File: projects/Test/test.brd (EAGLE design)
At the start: 65.8 x 27.6 mm, 45 parts, among them J1 284512-3, Y1 ECS-80-S-4X

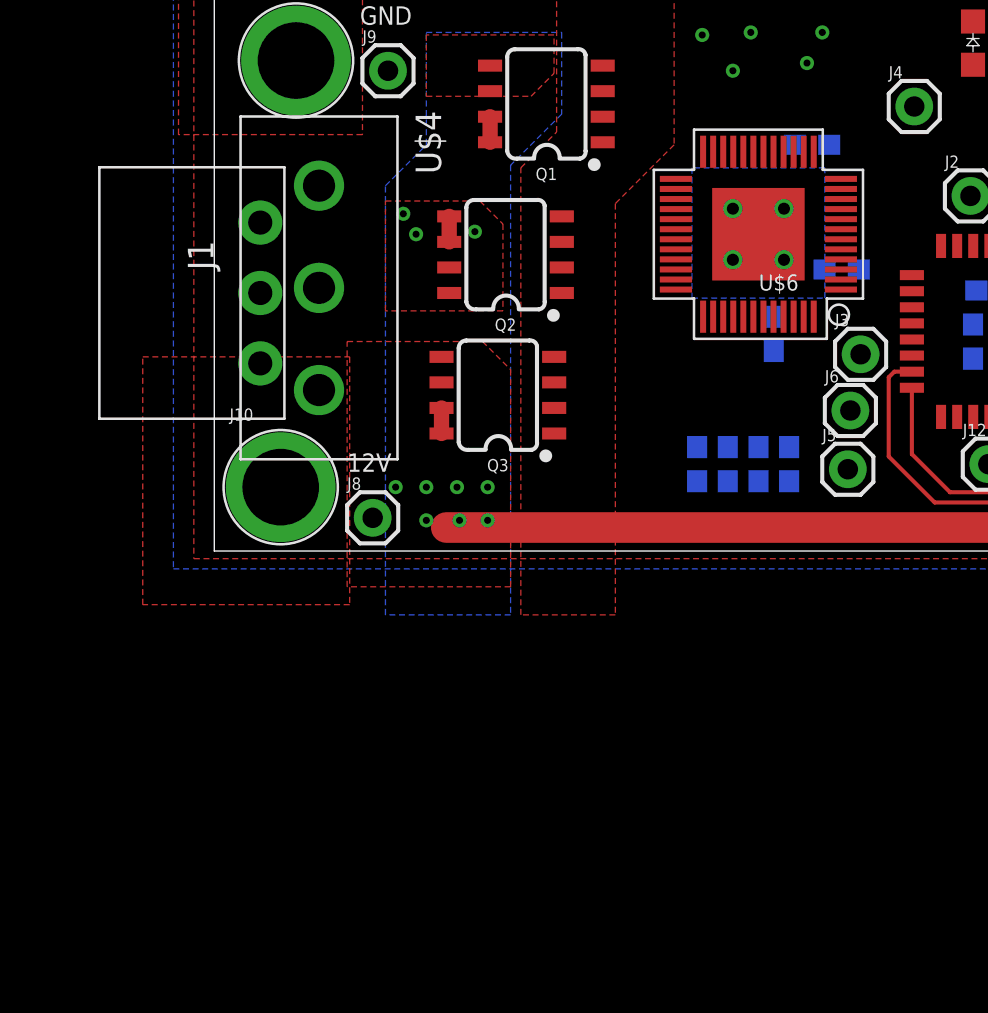
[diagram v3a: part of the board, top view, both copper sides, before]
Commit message: Switch to drv8343
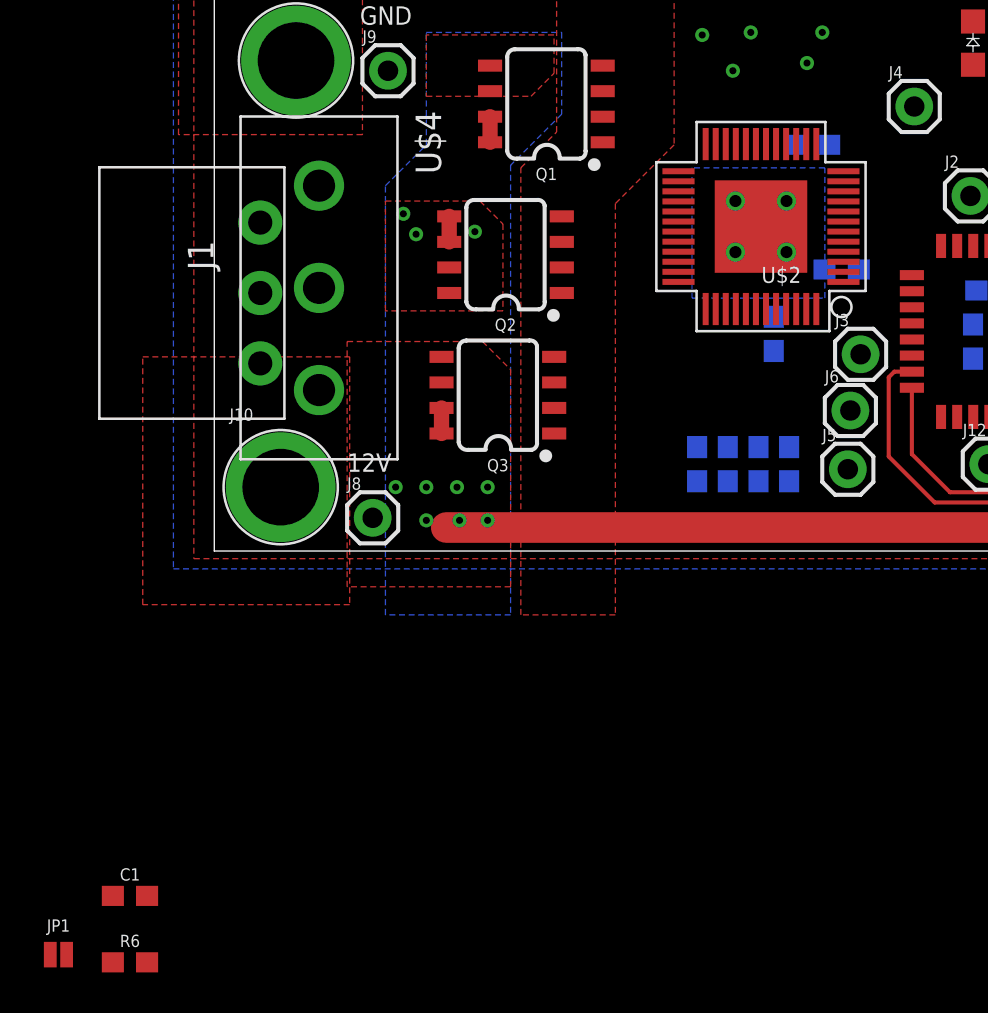
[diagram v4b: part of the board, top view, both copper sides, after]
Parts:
- removed U$6: DRV8340HBOTTOM-PAD, Motor Driver - DRV8340H:48-TQFP-BOTTOM
- added C1: 0.1uF, SparkFun-Capacitors:0603
- added JP1: JUMPER-SMT_2_NO_NO-SILK, SparkFun-Jumpers:SMT-JUMPER_2_NO_NO-SILK
- added R6: 47k, SparkFun-Resistors:0603
- added U$2: DRV8343H, Motor Driver - DRV834xH:48-TQFP-BOTTOM
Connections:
- new net !DIAG: U$2.40
- new net CAL: U$2.37, U$5.27
- new net GAIN: JP1.1, R6.2, U$2.35
- new net SNA: U$2.12
- new net SNB: U$2.13
- new net SNC: U$2.26
- new net SOA: U$2.29, U$5.8
- new net SOB: U$2.28, U$5.9
- new net SOC: U$2.27, U$5.11
- new net SPA: U$2.11
- new net SPB: U$2.14
- new net SPC: U$2.25
- net +3V3: now also C1.1, U$2.30
- net 12V: now also U$2.4, U$2.5; no longer U$6.4, U$6.5
- net 3V3_OUT: now also JP1.2, U$2.39; no longer U$6.39
- net CPH: now also U$2.2; no longer U$6.2
- net CPL: now also U$2.1; no longer U$6.1
- net EN_1: now also U$2.36; no longer U$6.36
- net FAULT_1: now also U$2.31; no longer U$6.31
- net GHA_1: now also U$2.6; no longer U$6.6
- net GHB_1: now also U$2.19; no longer U$6.19
- net GHC_1: now also U$2.20; no longer U$6.20
- net GLA_1: now also U$2.9; no longer U$6.9
- net GLB_1: now also U$2.16; no longer U$6.16
- net GLC_1: now also U$2.23; no longer U$6.23
- net GND: now also C1.2, R6.1, U$2.10, U$2.15, U$2.24, U$2.38, U$2.47, U$2.48, U$2.PAD, U$2.PAD_BOT, U$2.PAD_CON1, U$2.PAD_CON2, U$2.PAD_CON3, U$2.PAD_CON4; no longer U$6.10, U$6.11, U$6.12, U$6.13, U$6.14, U$6.15, U$6.24, U$6.25, U$6.26, U$6.27, U$6.28, U$6.29, U$6.30, U$6.37, U$6.38, U$6.47, U$6.48, U$6.PAD, U$6.PAD_BOT
- net IDRIVE: now also U$2.33; no longer U$6.33
- net INHA_1: now also U$2.41; no longer U$6.41
- net INHB_1: now also U$2.43; no longer U$6.43
- net INHC_1: now also U$2.45; no longer U$6.45
- net INLA_1: now also U$2.42; no longer U$6.42
- net INLB_1: now also U$2.44; no longer U$6.44
- net INLC_1: now also U$2.46; no longer U$6.46
- net MODE: now also U$2.32; no longer U$6.32
- net PHASE_A1: now also U$2.7, U$2.8; no longer U$6.7, U$6.8
- net PHASE_B1: now also U$2.17, U$2.18; no longer U$6.17, U$6.18
- net PHASE_C1: now also U$2.21, U$2.22; no longer U$6.21, U$6.22
- net VDS: now also U$2.34; no longer U$6.34
- net V_CAP_L: now also U$2.3; no longer U$6.3

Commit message: updated board
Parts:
- moved JP1 43.0 mm to (25.3, 7.11), turned to 270 degrees
- moved R6 39.3 mm to (23.0, 7.62)
- moved C1 38.2 mm to (22.9, 9.40), turned to 180 degrees
- moved C17 10.2 mm to (28.7, 23.5), turned to 180 degrees
- moved C15 8.64 mm to (28.8, 25.3)
- moved J3 6.58 mm to (31.0, 2.92)
- moved J7 5.40 mm to (35.7, 20.7)
- moved R7 5.26 mm to (22.9, 8.64), turned to 180 degrees
- moved J4 4.07 mm to (35.8, 17.8)
- moved C16 3.35 mm to (41.8, 11.2)
- moved C14 3.22 mm to (33.4, 15.9), turned to 90 degrees
- moved R5 3.07 mm to (49.0, 9.02)
- moved Y1 2.92 mm to (50.8, 8.66)
- moved J6 2.70 mm to (33.7, 4.83)
- moved R3 2.68 mm to (48.8, 7.44)
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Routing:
- net PHASE_A1: track 1.27 -> 31.2 mm
- net PHASE_C1: track 1.27 -> 29.5 mm
- net +3V3: track 1.85 -> 30.1 mm, vias 0 -> 3
- net PHASE_B1: track 1.27 -> 28.4 mm
- net 3V3_OUT: track 0.00 -> 23.5 mm, vias 0 -> 4
- net 12V: track 80.3 -> 102.8 mm, vias 10 -> 14
- net INLB_1: track 0.00 -> 20.8 mm
- net GND: track 0.00 -> 20.7 mm, vias 9 -> 13
- net INHB_1: track 0.00 -> 18.8 mm, vias 0 -> 1
- net FAULT_1: track 0.00 -> 17.2 mm, vias 0 -> 1
- net INLC_1: track 0.00 -> 16.9 mm
- net INLA_1: track 0.00 -> 15.0 mm, vias 0 -> 2
- net CAL: track 0.00 -> 14.9 mm, vias 0 -> 2
- net LED2: track 0.00 -> 14.8 mm, vias 0 -> 1
- net INHA_1: track 0.00 -> 14.1 mm, vias 0 -> 1
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
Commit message: updated test board
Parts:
- moved J2 1.53 mm to (38.6, 19.3)
- moved J4 0.68 mm to (35.6, 18.4)
- moved J7 0.52 mm to (35.6, 21.2)
- moved J12 0.51 mm to (38.1, 2.79)
- moved JP1 0.32 mm to (25.2, 6.79)
- moved C1 0.25 mm to (22.9, 9.14)
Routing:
- net SOB: track 0.00 -> 31.3 mm, vias 0 -> 2
- net SOC: track 0.00 -> 26.0 mm, vias 0 -> 2
- net SOA: track 0.00 -> 24.5 mm, vias 0 -> 3
- net +3V3: track 30.1 -> 49.5 mm, vias 3 -> 6
- net INHB_1: track 18.8 -> 23.0 mm, vias 1 -> 2
- net INLC_1: track 16.9 -> 19.9 mm
- net GND: track 20.7 -> 23.5 mm
- net INLA_1: track 15.0 -> 17.2 mm
- net INHA_1: track 14.1 -> 16.2 mm
- net FAULT_1: track 17.2 -> 18.3 mm, vias 1 -> 2
- net INHC_1: track 11.8 -> 12.9 mm
- net MODE: track 7.13 -> 8.03 mm
- net CAL: track 14.9 -> 15.6 mm

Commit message: Use no thermal banana con part. Remove DS Store
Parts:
- J10, J11: device SparkFun-Connectors:BANANA_CONN -> Banana Plug PTH:BANANA_CONN_NO_THERM
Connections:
- net 12V: now also J10.1; no longer J10.P$1
- net GND: now also J11.1; no longer J11.P$1
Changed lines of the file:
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@@
 <attribute name="VALUE" x="7.366" y="21.971" size="0.6096" layer="27" font="vector" ratio="20" align="top-left"/>
 </element>
-<element name="J10" library="SparkFun-Connectors" library_urn="urn:adsk.eagle:library:513" package="BANANA_CONN" package3d_urn="urn:adsk.eagle:package:38018/1" value="" x="3.302" y="2.794" smashed="yes">
+<element name="J10" library="Banana Plug PTH" package="BANANA_CONN_NO_THERM" value="" x="3.302" y="2.794" smashed="yes">
 <attribute name="NAME" x="0.762" y="6.096" size="0.6096" layer="25" font="vector" ratio="20"/>
 <attribute name="VALUE" x="0.762" y="-1.143" size="0.6096" layer="27" font="vector" ratio="20"/>
 </element>
-<element name="J11" library="SparkFun-Connectors" library_urn="urn:adsk.eagle:library:513" package="BANANA_CONN" package3d_urn="urn:adsk.eagle:package:38018/1" value="" x="4.064" y="24.003" smashed="yes">
+<element name="J11" library="Banana Plug PTH" package="BANANA_CONN_NO_THERM" value="" x="4.064" y="24.003" smashed="yes">
 <attribute name="NAME" x="1.524" y="27.305" size="0.6096" layer="25" font="vector" ratio="20"/>
 <attribute name="VALUE" x="1.524" y="20.066" size="0.6096" layer="27" font="vector" ratio="20"/>
@@
 <contactref element="SV1" pad="3"/>
 <contactref element="J9" pad="1"/>
-<contactref element="J11" pad="P$1"/>
+<contactref element="J11" pad="1"/>
 <contactref element="Q3" pad="1"/>
 <contactref element="Q2" pad="3"/>
@@
 <wire x1="38.543" y1="17.1541" x2="38.5445" y2="17.1556" width="0.2032" layer="1"/>
 <via x="38.5445" y="17.1556" extent="1-16" drill="0.35"/>
-<wire x1="27.178" y1="15.748" x2="28.448" y2="14.478" width="0" layer="19" extent="16-16"/>
+<wire x1="27.178" y1="15.748" x2="28.448" y2="14.478" width="0" layer="19" extent="1-1"/>
 <wire x1="27.178" y1="15.748" x2="27.178" y2="15.748" width="0" layer="19" extent="1-16"/>
 <wire x1="22.01" y1="9.144" x2="22.01" y2="8.636" width="0" layer="19" extent="1-16"/>
-<wire x1="25.908" y1="17.018" x2="27.178" y2="15.748" width="0" layer="19" extent="16-16"/>
+<wire x1="25.908" y1="17.018" x2="27.178" y2="15.748" width="0" layer="19" extent="1-1"/>
 </signal>
 <signal name="NRST">
@@
 <wire x1="61.722" y1="23.749" x2="64.389" y2="21.082" width="0.762" layer="1"/>
 <contactref element="J8" pad="1"/>
-<contactref element="J10" pad="P$1"/>
+<contactref element="J10" pad="1"/>
 <contactref element="Q3" pad="5"/>
 <contactref element="Q3" pad="6"/>
